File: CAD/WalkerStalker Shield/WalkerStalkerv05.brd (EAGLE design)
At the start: 49.5 x 53.3 mm, 25 parts

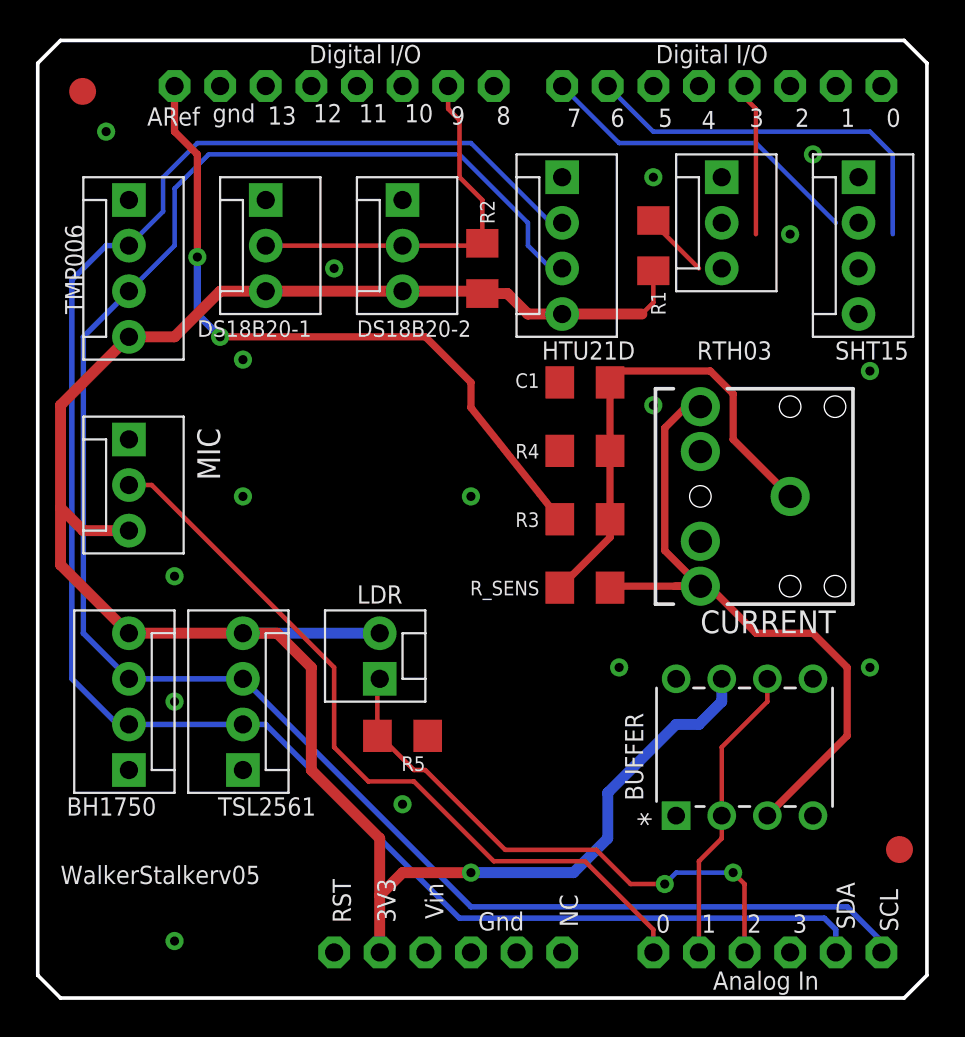
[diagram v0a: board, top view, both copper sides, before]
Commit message: Fixed Temperature sensors
+ Temperature sensors are now called by explicit address, rather than
index, which was not consistent (could not tell if sensor was wall or
air)
+ Unit IDs are not transmitted in data packets for easy identification
+Mounting bracket for TMP006 sensor added (3D file)
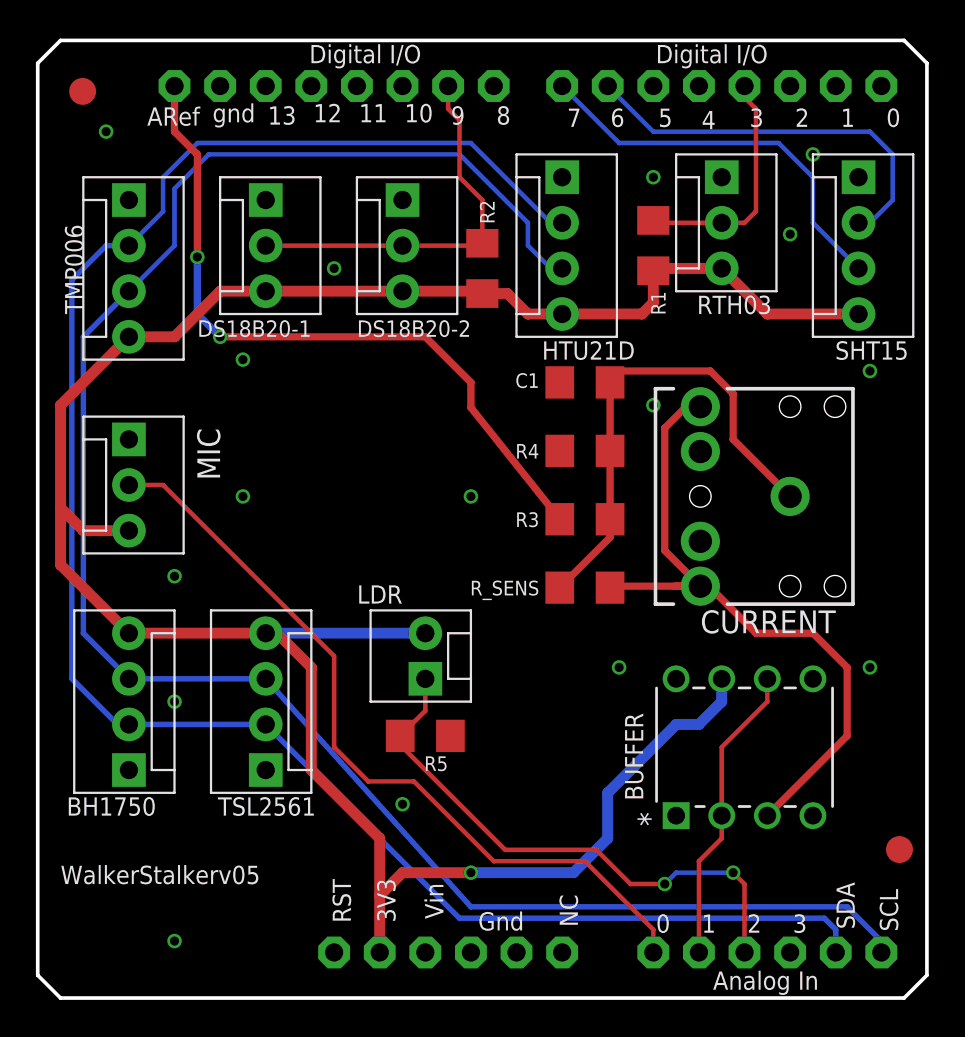
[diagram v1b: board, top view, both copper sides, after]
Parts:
- moved LDR 2.54 mm to (21.6, 17.8)
- moved R5 1.27 mm to (21.6, 14.6)
- moved TSL1 1.27 mm to (12.7, 12.7)
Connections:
- net D4 renamed TF-PWR
- net XBEE-PW renamed XBEE-PWR
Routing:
- net +3V3: track 119.1 -> 133.7 mm
- net SHT15-CL: track 18.4 -> 22.2 mm
- net RHT03: track 12.2 -> 13.4 mm
- net SHT15-DA: track 21.9 -> 22.4 mm
